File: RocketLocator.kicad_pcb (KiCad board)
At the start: 4 copper layers, 54 x 25 mm, 102 parts, among them J1 USB_C, J12 Battery / Switch, J2 Deploy Ch1 / Ch2, J3 Battery-, J4 Deploy Ch3 / Ch4, J7 U.FL-R-SMT(01), J8 Conn_ST_STDC14, Q1 2N7002KN, Q3 BSS84, U1 TPS22950YBHR, U11 PAM8904EGPR, U12 74HCS00, U13 DMP2021UFDF, U14 ISM6HG256XTR, U15 TPS22950YBHR, U16 MS5611-01BA, U17 MX25L6436F, U18 BQ25185DLHR, U2 SAM-M10Q-00B, U3 DRV5032DUDMRR, U4 CH340N, U5 STM32WL5MOCH6TR, U6 TPS22950YBHR, U7 RT9080-33GJ5, U8 TPS22950YBHR, U9 TPS22950YBHR

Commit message: Bundle project symbol and footprint libraries (#10)
* Bundle project symbol and footprint libraries

Adds the Custom symbol and footprint libraries from the personal KiCad 9.0
library folder, plus RT9080-33GJ5, STM32WL5MOCH6TR and U.FL-R-SMT_01_
symbols extracted from the schematic's embedded cache. Registers them in
project lib tables via ${KIPRJMOD} and adds a CI step that loads every
library so a broken file fails the build.

Co-Authored-By: Claude Opus 5.5 (1M context) <noreply@anthropic.com>
Claude-Session: https://claude.ai/code/session_01C1wUevCmefHv8PBPpeosyX

* Recover U7 and U17 footprints into Custom.pretty and relink

The RT9080 and Package_SO_New libraries are gone, so the footprints
were extracted from RocketLocator.kicad_pcb, un-flipped from B.Cu to
library (F.Cu) form, and added to lib/Custom.pretty. The schematic,
PCB and RT9080-33GJ5 symbol now point at Custom:.

Co-Authored-By: Claude Opus 5.5 (1M context) <noreply@anthropic.com>
Claude-Session: https://claude.ai/code/session_01C1wUevCmefHv8PBPpeosyX

---------

Co-authored-by: Claude <noreply@anthropic.com>
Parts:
- U17: footprint Package_SO_New:SOP-8_5.28x5.23mm_P1.27mm -> Custom:SOP-8_5.28x5.23mm_P1.27mm
- U7: footprint RT9080:SOT94P280X100-5N -> Custom:SOT94P280X100-5N
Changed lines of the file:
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@@
 		)
 	)
-	(footprint "RT9080:SOT94P280X100-5N"
+	(footprint "Custom:SOT94P280X100-5N"
 		(layer "B.Cu")
 		(at 40.78 33.9 -90)
@@
 		)
 	)
-	(footprint "Package_SO_New:SOP-8_5.28x5.23mm_P1.27mm"
+	(footprint "Custom:SOP-8_5.28x5.23mm_P1.27mm"
 		(layer "B.Cu")
 		(at 31.93 39.5 90)

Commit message: Swap J2/J4 deploy pinout, lower arm-gate pull-up, fix DRC errors
Schematic:
- J2 ch2 and J4 ch3/ch4 pin order changed: J2 pin 3 = DS2,
  pin 4 = DEPLOY2+; J4 pin 1 = DS3, pin 2 = DEPLOY3+, pin 3 = DS4,
  pin 4 = DEPLOY4+.
- R20 (U13 arm FET gate pull-up) 1M -> 100K.

PCB:
- Rerouted the deploy connectors for the new pinout.
- Connected Q5 pad 2 GND, which sat on an isolated B.Cu pour island
  (DRC "missing connection" on the GND zone).
- Updated U5 from the fixed LGA-92 library footprint (malformed
  courtyard errors).

DRC now reports no errors and no unconnected items. The remaining
ERC errors predate this change.

Co-Authored-By: Claude Opus 5.5 (1M context) <noreply@anthropic.com>
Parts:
- added Q4: PMXB43UNE, Custom:Nexperia_DFN1010D-3_SOT1215, B.Cu at (70.1, 33.8)
- added Q5: PMXB43UNE, Custom:Nexperia_DFN1010D-3_SOT1215, B.Cu at (70.1, 31.5)
- added Q6: PMXB43UNE, Custom:Nexperia_DFN1010D-3_SOT1215, B.Cu at (24.3, 33.2)
- added Q7: PMXB43UNE, Custom:Nexperia_DFN1010D-3_SOT1215, B.Cu at (24.3, 38.2)
- added R45: 100, Resistor_SMD:R_0402_1005Metric, B.Cu at (70.5, 36.6)
- added R46: 100, Resistor_SMD:R_0402_1005Metric, B.Cu at (70.0, 29.2)
- added R47: 100, Resistor_SMD:R_0402_1005Metric, B.Cu at (24.4, 31.9)
- added R48: 100, Resistor_SMD:R_0402_1005Metric, B.Cu at (24.4, 36.9)
- added R49: 100K, Resistor_SMD:R_0402_1005Metric, B.Cu at (70.0, 35.1)
- added R50: 100K, Resistor_SMD:R_0402_1005Metric, B.Cu at (70.0, 30.2)
- added R51: 100K, Resistor_SMD:R_0402_1005Metric, B.Cu at (24.4, 30.8)
- added R52: 100K, Resistor_SMD:R_0402_1005Metric, B.Cu at (24.4, 35.9)
- added R53: 1K, Resistor_SMD:R_0402_1005Metric, B.Cu at (70.5, 38.5)
- added R54: 1K, Resistor_SMD:R_0402_1005Metric, B.Cu at (70.0, 28.2)
- added R55: 1K, Resistor_SMD:R_0402_1005Metric, B.Cu at (24.4, 34.6)
- added R56: 1K, Resistor_SMD:R_0402_1005Metric, B.Cu at (24.3, 39.6)
- R20: value 1M -> 100K
- moved U15 2.17 mm to (70.6, 38.9), turned to 0 degrees
- moved R18 1.73 mm to (71.0, 40.1), turned to 180 degrees
- moved C2 1.38 mm to (69.6, 39.4), turned to 90 degrees
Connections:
- J2 pad 1: DS1 -> DEPLOY1+
- J2 pad 2: GND -> DS1
- J2 pad 4: GND -> DEPLOY2+
- J4 pad 2: GND -> DEPLOY3+
- J4 pad 4: GND -> DEPLOY4+
- U1 pad B2: DS3 -> DEPLOY3+
- U15 pad B2: DS1 -> DEPLOY1+
- U6 pad B2: DS2 -> DEPLOY2+
- U9 pad B2: DS4 -> DEPLOY4+
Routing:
- net DEPLOY3+: track 0.00 -> 7.91 mm
- net D2: track 43.5 -> 51.3 mm, vias 0 -> 1
- net DEPLOY2+: track 0.00 -> 7.33 mm
- net DEPLOY4+: track 0.00 -> 7.26 mm
- net D3: track 7.66 -> 14.2 mm, vias 0 -> 1
- net DEPLOY1+: track 0.00 -> 6.31 mm
- net D4: track 11.5 -> 17.4 mm, vias 0 -> 1
- net D1: track 41.4 -> 46.2 mm, vias 0 -> 1
- net DPWR: track 96.5 -> 93.1 mm
- net Net-(Q5-G): track 0.00 -> 3.13 mm
- net Net-(Q6-G): track 0.00 -> 2.39 mm
- net Net-(Q7-G): track 0.00 -> 2.38 mm
- net Net-(Q4-G): track 0.00 -> 2.32 mm
- net DS3: track 23.9 -> 21.6 mm
- net $SCL: track 44.3 -> 42.1 mm
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
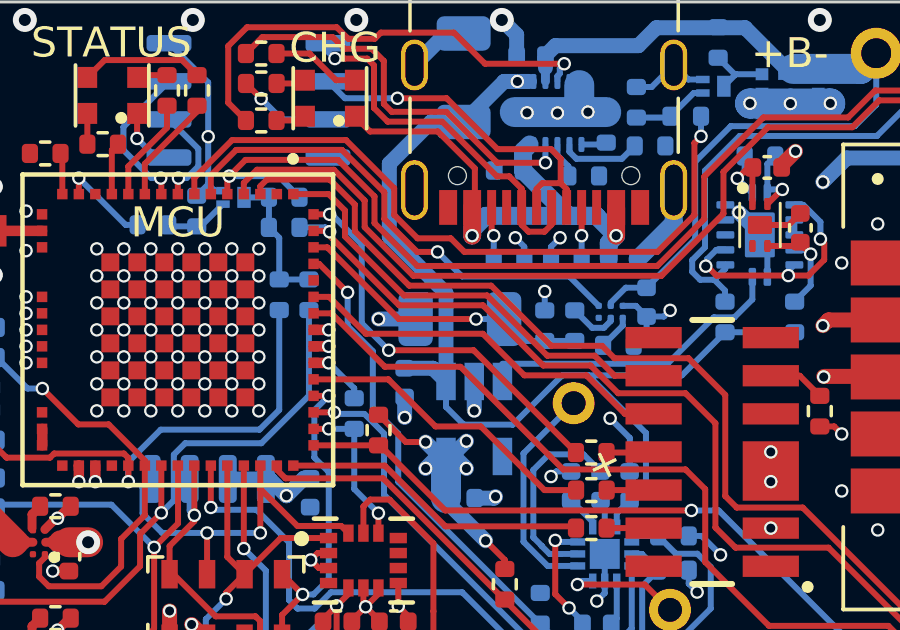
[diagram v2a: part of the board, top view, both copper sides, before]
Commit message: Move C7 (BATTLVL filter) to 0402 X7R
C7 only filters the battery-sense divider node (max ~3.2 V), so the
out-of-stock 50 V C0G 1206 part is not needed. Swap it to the same
0.1uF 0402 X7R as the other decoupling caps (C1525):
- Schematic footprint Capacitor_SMD:C_0402_1005Metric
- PCB: 0402 placed vertically on B.Cu at (41.775, 30.16) on the
  existing BATTLVL node; GND pad picks up the B.Cu pour. Old GND stub
  removed, zones refilled. DRC: 0 errors, 0 unconnected, schematic
  parity clean.
- BOM: C7 merged into the 0.1uF row, its own row removed.

Co-Authored-By: Claude Opus 5.5 (1M context) <noreply@anthropic.com>
Claude-Session: https://claude.ai/code/session_01Qn4Fhe37cECFfk8PPTy8Kj
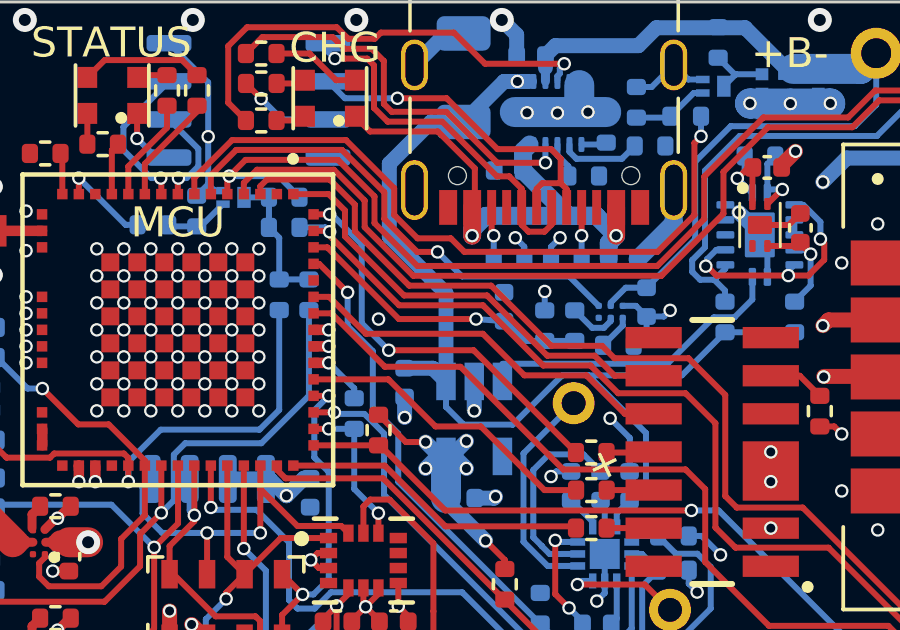
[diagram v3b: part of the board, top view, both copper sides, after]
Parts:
- C7: footprint Capacitor_SMD:C_1206_3216Metric -> Capacitor_SMD:C_0402_1005Metric
- moved C7 1.53 mm to (41.8, 30.2), turned to 90 degrees
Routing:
- net GND: track 55.6 -> 54.4 mm
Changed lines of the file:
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@@
 		)
 	)
+	(footprint "Capacitor_SMD:C_0402_1005Metric"
+		(layer "B.Cu")
+		(at 41.775 30.16 90)
+		(descr "Capacitor SMD 0402 (1005 Metric), square (rectangular) end terminal, IPC-7351 nominal, (Body size source: IPC-SM-782 page 76, https://www.pcb-3d.com/wordpress/wp-content/uploads/ipc-sm-782a_amendment_1_and_2.pdf), generated with kicad-footprint-generator")
+		(tags "capacitor")
+		(property "Reference" "C7"
+			(at 0 1.16 90)
+			(layer "B.SilkS")
+			(hide yes)
+			(effects
+				(font
+					(size 1 1)
+					(thickness 0.15)
+				)
+				(justify mirror)
+			)
+		)
+		(property "Value" "0.1uF"
+			(at 0 -1.16 90)
+			(layer "B.Fab")
+			(effects
+				(font
+					(size 1 1)
+					(thickness 0.15)
+				)
+				(justify mirror)
+			)
+		)
+		(property "Datasheet" ""
+			(at 0 0 90)
+			(layer "B.Fab")
+			(hide yes)
+			(effects
+				(font
+					(size 1.27 1.27)
+					(thickness 0.15)
+				)
+				(justify mirror)
+			)
+		)
+		(property "Description" ""
+			(at 0 0 90)
+			(layer "B.Fab")
+			(hide yes)
+			(effects
+				(font
+					(size 1.27 1.27)
+					(thickness 0.15)
+				)
+				(justify mirror)
+			)
+		)
+		(property ki_fp_filters "C_*")
+		(sheetname "/")
+		(sheetfile "RocketLocator.kicad_sch")
+		(units
+			(unit
+				(name "A")
+				(pins "1" "2")
+			)
+		)
+		(attr smd)
+		(duplicate_pad_numbers_are_jumpers no)
+		(fp_line
+			(start -0.107836 -0.36)
+			(end 0.107836 -0.36)
+			(stroke
+				(width 0.12)
+				(type solid)
+			)
+			(layer "B.SilkS")
+		)
+		(fp_line
+			(start -0.107836 0.36)
+			(end 0.107836 0.36)
+			(stroke
+				(width 0.12)
+				(type solid)
+			)
+			(layer "B.SilkS")
+		)
+		(fp_line
+			(start 0.91 -0.46)
+			(end -0.91 -0.46)
+			(stroke
+				(width 0.05)
+				(type solid)
+			)
+			(layer "B.CrtYd")
+		)
+		(fp_line
+			(start -0.91 -0.46)
+			(end -0.91 0.46)
+			(stroke
+				(width 0.05)
+				(type solid)
+			)
+			(layer "B.CrtYd")
+		)
+		(fp_line
+			(start 0.91 0.46)
+			(end 0.91 -0.46)
+			(stroke
+				(width 0.05)
+				(type solid)
+			)
+			(layer "B.CrtYd")
+		)
+		(fp_line
+			(start -0.91 0.46)
+			(end 0.91 0.46)
+			(stroke
+				(width 0.05)
+				(type solid)
+			)
+			(layer "B.CrtYd")
+		)
+		(fp_line
+			(start 0.5 -0.25)
+			(end -0.5 -0.25)
+			(stroke
+				(width 0.1)
+				(type solid)
+			)
+			(layer "B.Fab")
+		)
+		(fp_line
+			(start -0.5 -0.25)
+			(end -0.5 0.25)
+			(stroke
+				(width 0.1)
+				(type solid)
+			)
+			(layer "B.Fab")
+		)
+		(fp_line
+			(start 0.5 0.25)
+			(end 0.5 -0.25)
+			(stroke
+				(width 0.1)
+				(type solid)
+			)
+			(layer "B.Fab")
+		)
+		(fp_line
+			(start -0.5 0.25)
+			(end 0.5 0.25)
+			(stroke
+				(width 0.1)
+				(type solid)
+			)
+			(layer "B.Fab")
+		)
+		(fp_text user "${REFERENCE}"
+			(at 0 0 90)
+			(layer "B.Fab")
+			(effects
+				(font
+					(size 0.25 0.25)
+					(thickness 0.04)
+				)
+				(justify mirror)
+			)
+		)
+		(pad "1" smd roundrect
+			(at -0.48 0 90)
+			(size 0.56 0.62)
+			(layers "B.Cu" "B.Mask" "B.Paste")
+			(roundrect_rratio 0.25)
+			(net "BATTLVL")
+			(pintype "passive")
+		)
+		(pad "2" smd roundrect
+			(at 0.48 0 90)
+			(size 0.56 0.62)
+			(layers "B.Cu" "B.Mask" "B.Paste")
+			(roundrect_rratio 0.25)
+			(net "GND")
+			(pintype "passive")
+		)
+		(embedded_fonts no)
+		(model "${KICAD9_3DMODEL_DIR}/Capacitor_SMD.3dshapes/C_0402_1005Metric.step"
+			(offset
+				(xyz 0 0 0)
+			)
+			(scale
+				(xyz 1 1 1)
+			)
+			(rotate
+				(xyz 0 0 0)
+			)
+		)
+	)
 	(footprint "Resistor_SMD:R_0402_1005Metric"
 		(layer "B.Cu")
@@
 		(embedded_fonts no)
 	)
-	(footprint "Capacitor_SMD:C_1206_3216Metric"
-		(layer "B.Cu")
-		(at 40.3 30.57 180)
-		(descr "Capacitor SMD 1206 (3216 Metric), square (rectangular) end terminal, IPC-7351 nominal, (Body size source: IPC-SM-782 page 76, https://www.pcb-3d.com/wordpress/wp-content/uploads/ipc-sm-782a_amendment_1_and_2.pdf), generated with kicad-footprint-generator")
-		(tags "capacitor")
-		(property "Reference" "C7"
-			(at 0 1.85 0)
-			(layer "B.SilkS")
-			(hide yes)
-			(effects
-				(font
-					(size 1 1)
-					(thickness 0.15)
-				)
-				(justify mirror)
-			)
-		)
-		(property "Value" "0.1uF"
-			(at 0 -1.85 0)
-			(layer "B.Fab")
-			(effects
-				(font
-					(size 1 1)
-					(thickness 0.15)
-				)
-				(justify mirror)
-			)
-		)
-		(property "Datasheet" ""
-			(at 0 0 0)
-			(layer "B.Fab")
-			(hide yes)
-			(effects
-				(font
-					(size 1.27 1.27)
-					(thickness 0.15)
-				)
-				(justify mirror)
-			)
-		)
-		(property "Description" ""
-			(at 0 0 0)
-			(layer "B.Fab")
-			(hide yes)
-			(effects
-				(font
-					(size 1.27 1.27)
-					(thickness 0.15)
-				)
-				(justify mirror)
-			)
-		)
-		(property ki_fp_filters "C_*")
-		(sheetname "/")
-		(sheetfile "RocketLocator.kicad_sch")
-		(units
-			(unit
-				(name "A")
-				(pins "1" "2")
-			)
-		)
-		(attr smd)
-		(duplicate_pad_numbers_are_jumpers no)
-		(fp_line
-			(start -0.711252 0.91)
-			(end 0.711252 0.91)
-			(stroke
-				(width 0.12)
-				(type solid)
-			)
-			(layer "B.SilkS")
-		)
-		(fp_line
-			(start -0.711252 -0.91)
-			(end 0.711252 -0.91)
-			(stroke
-				(width 0.12)
-				(type solid)
-			)
-			(layer "B.SilkS")
-		)
-		(fp_line
-			(start 2.3 1.15)
-			(end 2.3 -1.15)
-			(stroke
-				(width 0.05)
-				(type solid)
-			)
-			(layer "B.CrtYd")
-		)
-		(fp_line
-			(start 2.3 -1.15)
-			(end -2.3 -1.15)
-			(stroke
-				(width 0.05)
-				(type solid)
-			)
-			(layer "B.CrtYd")
-		)
-		(fp_line
-			(start -2.3 1.15)
-			(end 2.3 1.15)
-			(stroke
-				(width 0.05)
-				(type solid)
-			)
-			(layer "B.CrtYd")
-		)
-		(fp_line
-			(start -2.3 -1.15)
-			(end -2.3 1.15)
-			(stroke
-				(width 0.05)
-				(type solid)
-			)
-			(layer "B.CrtYd")
-		)
-		(fp_line
-			(start 1.6 0.8)
-			(end 1.6 -0.8)
-			(stroke
-				(width 0.1)
-				(type solid)
-			)
-			(layer "B.Fab")
-		)
-		(fp_line
-			(start 1.6 -0.8)
-			(end -1.6 -0.8)
-			(stroke
-				(width 0.1)
-				(type solid)
-			)
-			(layer "B.Fab")
-		)
-		(fp_line
-			(start -1.6 0.8)
-			(end 1.6 0.8)
-			(stroke
-				(width 0.1)
-				(type solid)
-			)
-			(layer "B.Fab")
-		)
-		(fp_line
-			(start -1.6 -0.8)
-			(end -1.6 0.8)
-			(stroke
-				(width 0.1)
-				(type solid)
-			)
-			(layer "B.Fab")
-		)
-		(fp_text user "${REFERENCE}"
-			(at 0 0 0)
-			(layer "B.Fab")
-			(effects
-				(font
-					(size 0.8 0.8)
-					(thickness 0.12)
-				)
-				(justify mirror)
-			)
-		)
-		(pad "1" smd roundrect
-			(at -1.475 0 180)
-			(size 1.15 1.8)
-			(layers "B.Cu" "B.Mask" "B.Paste")
-			(roundrect_rratio 0.217391)
-			(net "BATTLVL")
-			(pintype "passive")
-		)
-		(pad "2" smd roundrect
-			(at 1.475 0 180)
-			(size 1.15 1.8)
-			(layers "B.Cu" "B.Mask" "B.Paste")
-			(roundrect_rratio 0.217391)
-			(net "GND")
-			(pintype "passive")
-		)
-		(embedded_fonts no)
-		(model "${KICAD9_3DMODEL_DIR}/Capacitor_SMD.3dshapes/C_1206_3216Metric.step"
-			(offset
-				(xyz 0 0 0)
-			)
-			(scale
-				(xyz 1 1 1)
-			)
-			(rotate
-				(xyz 0 0 0)
-			)
-		)
-	)
 	(footprint "Resistor_SMD:R_0402_1005Metric"
 		(layer "B.Cu")
@@
 	)
 	(segment
-		(start 38.825 30.57)
-		(end 37.59 30.57)
-		(width 0.5)
-		(layer "B.Cu")
-		(net "GND")
-	)
-	(segment
 		(start 39.839761 21.050239)
 		(end 38.79 22.1)
@@
 	)
 	(segment
-		(start 41.775 30.57)
+		(start 41.775 30.64)
 		(end 40.84 30.57)
 		(width 0.2)
@@
 	(segment
 		(start 42.505 31.3)
-		(end 41.775 30.57)
+		(end 41.775 30.64)
 		(width 0.2)
 		(layer "B.Cu")

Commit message: Reposition components (Frank's layout changes)
Co-Authored-By: Claude Opus 5.5 (1M context) <noreply@anthropic.com>
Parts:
- moved C7 0.75 mm to (42.1, 30.8)
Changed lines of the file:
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@@
 	(footprint "Capacitor_SMD:C_0402_1005Metric"
 		(layer "B.Cu")
-		(at 41.775 30.16 90)
+		(at 42.14 30.82 90)
 		(descr "Capacitor SMD 0402 (1005 Metric), square (rectangular) end terminal, IPC-7351 nominal, (Body size source: IPC-SM-782 page 76, https://www.pcb-3d.com/wordpress/wp-content/uploads/ipc-sm-782a_amendment_1_and_2.pdf), generated with kicad-footprint-generator")
 		(tags "capacitor")
@@
 	)
 	(segment
-		(start 44.519557 32.446918)
-		(end 45.802639 33.73)
+		(start 45.802639 33.73)
+		(end 46.76 33.73)
 		(width 0.2)
 		(layer "F.Cu")
@@
 	)
 	(segment
-		(start 37.17 31.06)
-		(end 41.066164 31.06)
+		(start 35.425 29.83)
+		(end 35.94 29.83)
 		(width 0.2)
 		(layer "F.Cu")
@@
 	)
 	(segment
-		(start 42.453082 32.446918)
-		(end 44.519557 32.446918)
+		(start 40.16 31.06)
+		(end 41.546918 32.446918)
 		(width 0.2)
 		(layer "F.Cu")
@@
 	)
 	(segment
-		(start 41.066164 31.06)
-		(end 42.453082 32.446918)
+		(start 41.546918 32.446918)
+		(end 44.519557 32.446918)
 		(width 0.2)
 		(layer "F.Cu")
@@
 	)
 	(segment
-		(start 45.802639 33.73)
-		(end 46.76 33.73)
+		(start 37.17 31.06)
+		(end 40.16 31.06)
 		(width 0.2)
 		(layer "F.Cu")
@@
 	)
 	(segment
-		(start 35.94 29.83)
-		(end 37.17 31.06)
+		(start 44.519557 32.446918)
+		(end 45.802639 33.73)
 		(width 0.2)
 		(layer "F.Cu")
@@
 	)
 	(segment
-		(start 35.425 29.83)
-		(end 35.94 29.83)
+		(start 35.94 29.83)
+		(end 37.17 31.06)
 		(width 0.2)
 		(layer "F.Cu")
@@
 	)
 	(segment
-		(start 38.27 30.57)
-		(end 40.84 30.57)
+		(start 40.7 30.57)
+		(end 41.43 31.3)
 		(width 0.2)
 		(layer "F.Cu")
@@
 		(net "BATTLVL")
 	)
-	(via
-		(at 40.84 30.57)
-		(size 0.45)
-		(drill 0.3)
-		(layers "F.Cu" "B.Cu")
-		(capping no)
-		(covering
-			(front no)
-			(back no)
-		)
-		(plugging
-			(front no)
-			(back no)
-		)
-		(filling no)
-		(net "BATTLVL")
-	)
 	(segment
-		(start 43.13 31.3)
-		(end 42.505 31.3)
+		(start 38.27 30.57)
+		(end 40.7 30.57)
 		(width 0.2)
-		(layer "B.Cu")
+		(layer "F.Cu")
 		(net "BATTLVL")
 	)
-	(segment
-		(start 41.775 30.64)
-		(end 40.84 30.57)
-		(width 0.2)
-		(layer "B.Cu")
+	(via
+		(at 41.43 31.3)
+		(size 0.45)
+		(drill 0.3)
+		(layers "F.Cu" "B.Cu")
+		(free yes)
 		(net "BATTLVL")
 	)
 	(segment
-		(start 42.505 31.3)
-		(end 41.775 30.64)
+		(start 44.13 31.3)
+		(end 41.43 31.3)
 		(width 0.2)
 		(layer "B.Cu")
@@
 	)
 	(segment
-		(start 44.13 31.3)
-		(end 43.13 31.3)
+		(start 35.425 27.08)
+		(end 35.96 27.08)
 		(width 0.2)
-		(layer "B.Cu")
-		(net "BATTLVL")
+		(layer "F.Cu")
+		(net "$SWO")
 	)
 	(segment
-		(start 40.76 31.61)
+		(start 40.24 31.61)
 		(end 37.93 31.61)
 		(width 0.2)
@@
 	(segment
 		(start 44.17 35.02)
-		(end 40.76 31.61)
+		(end 43.65 35.02)
 		(width 0.2)
 		(layer "F.Cu")
@@
 	)
 	(segment
-		(start 35.425 27.08)
-		(end 35.96 27.08)
+		(start 43.65 35.02)
+		(end 40.24 31.61)
 		(width 0.2)
 		(layer "F.Cu")
